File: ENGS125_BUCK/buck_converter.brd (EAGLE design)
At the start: 75.9 x 62.2 mm, 19 parts, among them M1 IPD220N06L3, M2 IPD220N06L3, U1 LTC6992, U2 LTC4449

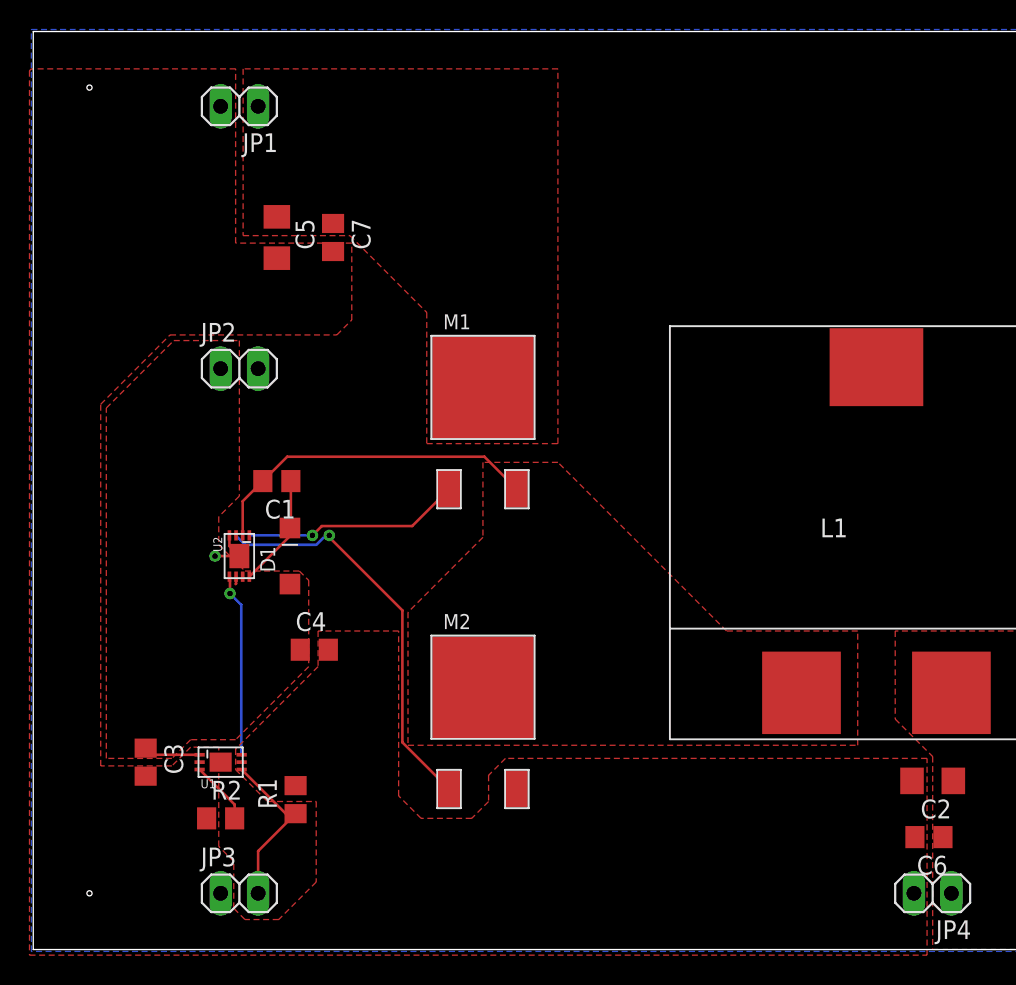
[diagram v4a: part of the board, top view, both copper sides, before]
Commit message: Cleaned up polygons and top layer routing
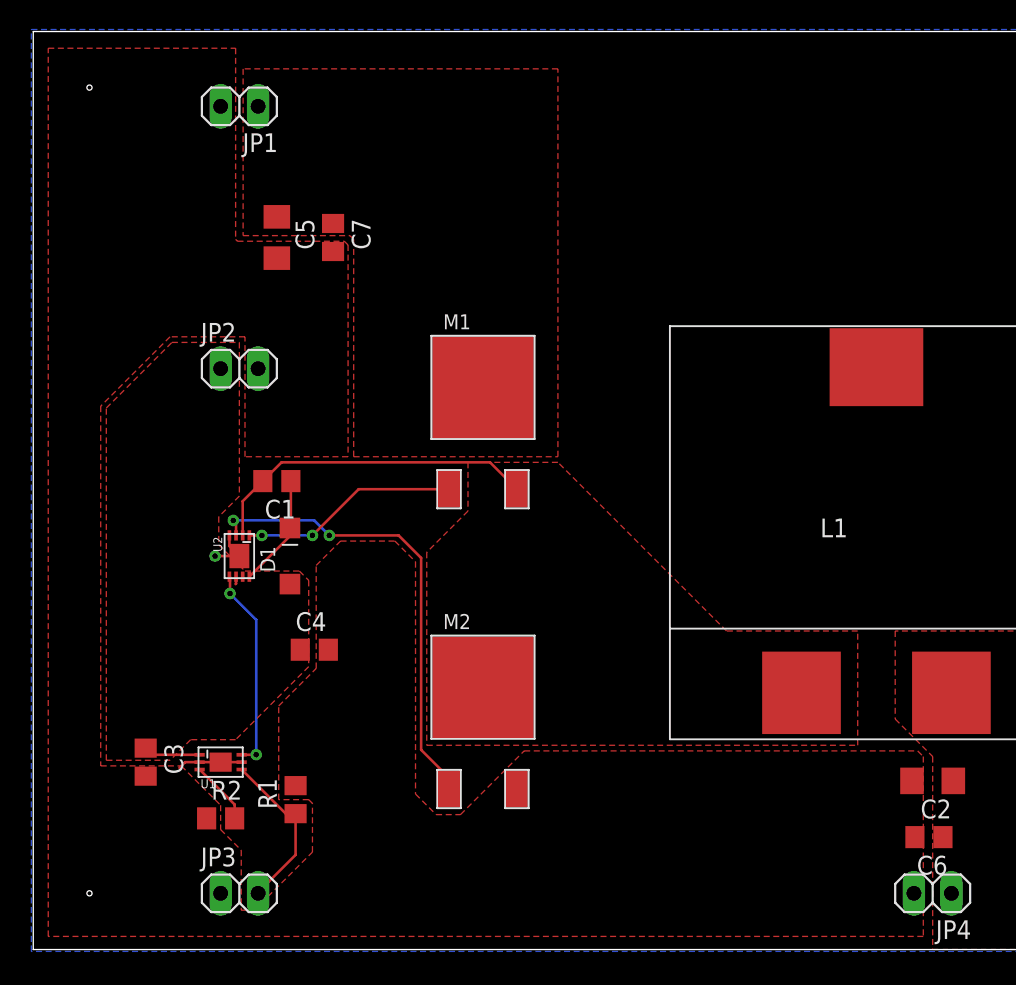
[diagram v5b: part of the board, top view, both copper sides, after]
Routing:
- net GND: track 3.33 -> 7.71 mm
- net BG: track 27.4 -> 31.3 mm, vias 1 -> 2
- net VPWM: track 12.4 -> 13.8 mm, vias 1 -> 2
- net TG: track 14.7 -> 14.8 mm, vias 1 -> 2
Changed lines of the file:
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@@
 <contactref element="U1" pad="5"/>
 <contactref element="U1" pad="7"/>
-<polygon width="0.1524" layer="1" isolate="0.00030625" thermals="no">
-<vertex x="13.716" y="47.879"/>
-<vertex x="13.716" y="59.69"/>
-<vertex x="-0.127" y="59.69"/>
-<vertex x="-0.254" y="59.563"/>
-<vertex x="-0.254" y="-0.381"/>
-<vertex x="60.579" y="-0.381"/>
-<vertex x="60.579" y="12.954"/>
-<vertex x="32.004" y="12.954"/>
-<vertex x="30.861" y="11.811"/>
-<vertex x="30.861" y="10.033"/>
-<vertex x="29.718" y="8.89"/>
-<vertex x="26.289" y="8.89"/>
-<vertex x="24.765" y="10.414"/>
-<vertex x="24.765" y="21.59"/>
-<vertex x="19.304" y="21.59"/>
-<vertex x="19.304" y="19.177"/>
-<vertex x="13.716" y="13.589"/>
-<vertex x="13.716" y="12.192"/>
-<vertex x="15.875" y="10.033"/>
-<vertex x="19.177" y="10.033"/>
-<vertex x="19.177" y="4.572"/>
-<vertex x="16.637" y="2.032"/>
-<vertex x="14.351" y="2.032"/>
-<vertex x="13.589" y="2.794"/>
-<vertex x="13.589" y="5.969"/>
-<vertex x="12.573" y="6.985"/>
-<vertex x="12.573" y="13.716"/>
-<vertex x="10.668" y="13.716"/>
-<vertex x="9.398" y="12.446"/>
-<vertex x="4.572" y="12.446"/>
-<vertex x="4.572" y="36.957"/>
-<vertex x="9.271" y="41.656"/>
-<vertex x="20.574" y="41.656"/>
-<vertex x="21.59" y="42.672"/>
-<vertex x="21.59" y="47.879"/>
-</polygon>
 <polygon width="0.1524" layer="16" isolate="0.00030625" thermals="no">
 <vertex x="-0.127" y="62.357"/>
@@
 <wire x1="13.97" y1="26.67" x2="12.319" y2="26.67" width="0.1778" layer="1"/>
 <via x="12.319" y="26.67" extent="1-16" drill="0.381"/>
+<polygon width="0.1778" layer="1" isolate="0.00030625" thermals="no">
+<vertex x="60.325" y="13.081"/>
+<vertex x="60.325" y="0.889"/>
+<vertex x="1.016" y="0.889"/>
+<vertex x="1.016" y="61.087"/>
+<vertex x="13.716" y="61.087"/>
+<vertex x="13.716" y="48.133"/>
+<vertex x="13.843" y="48.006"/>
+<vertex x="21.082" y="48.006"/>
+<vertex x="21.336" y="47.752"/>
+<vertex x="21.336" y="33.401"/>
+<vertex x="14.351" y="33.401"/>
+<vertex x="14.351" y="41.529"/>
+<vertex x="9.271" y="41.529"/>
+<vertex x="4.572" y="36.83"/>
+<vertex x="4.572" y="12.446"/>
+<vertex x="10.033" y="12.446"/>
+<vertex x="12.7" y="9.779"/>
+<vertex x="12.7" y="8.128"/>
+<vertex x="14.097" y="6.731"/>
+<vertex x="14.097" y="2.667"/>
+<vertex x="14.986" y="2.667"/>
+<vertex x="18.923" y="6.604"/>
+<vertex x="18.923" y="9.906"/>
+<vertex x="18.669" y="10.16"/>
+<vertex x="16.637" y="10.16"/>
+<vertex x="16.637" y="16.51"/>
+<vertex x="19.177" y="19.05"/>
+<vertex x="19.177" y="26.035"/>
+<vertex x="20.828" y="27.686"/>
+<vertex x="24.511" y="27.686"/>
+<vertex x="25.908" y="26.289"/>
+<vertex x="25.908" y="10.541"/>
+<vertex x="27.305" y="9.144"/>
+<vertex x="28.956" y="9.144"/>
+<vertex x="33.274" y="13.462"/>
+<vertex x="59.944" y="13.462"/>
+</polygon>
+<wire x1="11.275" y1="12.7" x2="10.287" y2="12.7" width="0.1778" layer="1"/>
+<wire x1="10.287" y1="12.7" x2="9.906" y2="12.319" width="0.1778" layer="1"/>
+<wire x1="14.125" y1="12.7" x2="12.7" y2="12.7" width="0.1778" layer="1"/>
+<wire x1="12.7" y1="12.7" x2="11.275" y2="12.7" width="0.1778" layer="1"/>
 </signal>
 <signal name="VGG">
@@
 <contactref element="U2" pad="6"/>
 <polygon width="0.1778" layer="1" isolate="0.00030625" thermals="no">
-<vertex x="13.97" y="41.275"/>
+<vertex x="13.97" y="41.148"/>
 <vertex x="13.97" y="30.734"/>
 <vertex x="12.573" y="29.337"/>
@@
 <vertex x="13.716" y="14.224"/>
 <vertex x="10.668" y="14.224"/>
-<vertex x="9.398" y="12.954"/>
-<vertex x="4.953" y="12.954"/>
+<vertex x="9.271" y="12.827"/>
+<vertex x="4.953" y="12.827"/>
 <vertex x="4.953" y="36.703"/>
-<vertex x="9.525" y="41.275"/>
+<vertex x="9.398" y="41.148"/>
 </polygon>
 <wire x1="13.745" y1="25.27" x2="13.745" y2="24.794" width="0.1778" layer="1"/>
@@
 <wire x1="13.295" y1="25.27" x2="13.335" y2="25.23" width="0.1778" layer="1"/>
 <via x="13.335" y="24.13" extent="1-16" drill="0.381"/>
-<wire x1="13.335" y1="24.13" x2="14.097" y2="23.368" width="0.1778" layer="16"/>
-<wire x1="14.097" y1="23.368" x2="14.097" y2="13.208" width="0.1778" layer="16"/>
+<wire x1="13.335" y1="24.13" x2="15.113" y2="22.352" width="0.1778" layer="16"/>
+<wire x1="15.113" y1="22.352" x2="15.113" y2="13.208" width="0.1778" layer="16"/>
 <wire x1="13.335" y1="25.23" x2="13.335" y2="24.13" width="0.1778" layer="1"/>
-<wire x1="14.097" y1="13.208" x2="14.125" y2="13.2" width="0" layer="19" extent="1-16"/>
+<via x="15.113" y="13.208" extent="1-16" drill="0.381"/>
+<wire x1="15.113" y1="13.208" x2="15.105" y2="13.2" width="0.1778" layer="1"/>
+<wire x1="15.105" y1="13.2" x2="14.125" y2="13.2" width="0.1778" layer="1"/>
 </signal>
 <signal name="VMOD">
@@
 <contactref element="R1" pad="1"/>
 <contactref element="JP3" pad="2"/>
-<wire x1="15.24" y1="3.81" x2="15.24" y2="6.67" width="0.1778" layer="1"/>
-<wire x1="15.24" y1="6.67" x2="17.78" y2="9.21" width="0.1778" layer="1"/>
+<wire x1="15.24" y1="3.81" x2="15.24" y2="3.876" width="0.1778" layer="1"/>
+<wire x1="17.78" y1="6.416" x2="15.24" y2="3.876" width="0.1778" layer="1"/>
+<wire x1="17.78" y1="6.416" x2="17.78" y2="9.21" width="0.1778" layer="1"/>
 <wire x1="14.125" y1="12.2" x2="17.115" y2="9.21" width="0.1778" layer="1"/>
 <wire x1="17.115" y1="9.21" x2="17.78" y2="9.21" width="0.1778" layer="1"/>
@@
 <contactref element="U2" pad="2"/>
 <polygon width="0.1524" layer="1" isolate="0.00030625" thermals="no">
-<vertex x="25.4" y="22.86"/>
-<vertex x="25.4" y="13.843"/>
+<vertex x="26.67" y="26.924"/>
+<vertex x="26.67" y="13.843"/>
 <vertex x="55.88" y="13.843"/>
 <vertex x="55.88" y="21.59"/>
 <vertex x="46.99" y="21.59"/>
 <vertex x="35.56" y="33.02"/>
-<vertex x="30.48" y="33.02"/>
-<vertex x="30.48" y="27.94"/>
+<vertex x="29.464" y="33.02"/>
+<vertex x="29.464" y="29.718"/>
 </polygon>
-<wire x1="32.78" y1="31.2" x2="30.579" y2="33.401" width="0.1778" layer="1"/>
-<wire x1="30.579" y1="33.401" x2="17.211" y2="33.401" width="0.1778" layer="1"/>
-<wire x1="17.211" y1="33.401" x2="15.56" y2="31.75" width="0.1778" layer="1"/>
+<wire x1="32.78" y1="31.2" x2="30.96" y2="33.02" width="0.1778" layer="1"/>
+<wire x1="30.96" y1="33.02" x2="16.83" y2="33.02" width="0.1778" layer="1"/>
+<wire x1="16.83" y1="33.02" x2="15.56" y2="31.75" width="0.1778" layer="1"/>
 <wire x1="15.56" y1="31.75" x2="14.195" y2="30.385" width="0.1778" layer="1"/>
 <wire x1="14.195" y1="30.385" x2="14.195" y2="28.07" width="0.1778" layer="1"/>
@@
 <vertex x="14.224" y="48.387"/>
 <vertex x="21.463" y="48.387"/>
-<vertex x="26.67" y="43.18"/>
-<vertex x="26.67" y="34.29"/>
-<vertex x="35.56" y="34.29"/>
+<vertex x="21.717" y="48.133"/>
+<vertex x="21.717" y="33.401"/>
+<vertex x="35.56" y="33.401"/>
 <vertex x="35.56" y="59.69"/>
 </polygon>
@@
 <contactref element="U2" pad="3"/>
 <contactref element="M2" pad="G"/>
-<wire x1="28.18" y1="10.88" x2="25.019" y2="14.041" width="0.1778" layer="1"/>
-<wire x1="25.019" y1="14.041" x2="25.019" y2="22.987" width="0.1778" layer="1"/>
-<wire x1="25.019" y1="22.987" x2="20.066" y2="27.94" width="0.1778" layer="1"/>
-<wire x1="20.066" y1="27.94" x2="20.066" y2="28.067" width="0.1778" layer="1"/>
+<wire x1="28.18" y1="10.88" x2="28.18" y2="11.642" width="0.1778" layer="1"/>
+<wire x1="28.18" y1="11.642" x2="26.289" y2="13.533" width="0.1778" layer="1"/>
+<wire x1="26.289" y1="13.533" x2="26.289" y2="26.543" width="0.1778" layer="1"/>
+<wire x1="20.066" y1="28.067" x2="24.765" y2="28.067" width="0.1778" layer="1"/>
+<wire x1="26.289" y1="26.543" x2="24.765" y2="28.067" width="0.1778" layer="1"/>
 <via x="20.066" y="28.067" extent="1-16" drill="0.381"/>
-<wire x1="20.066" y1="28.067" x2="19.82103125" y2="28.067" width="0.1778" layer="16"/>
-<wire x1="19.82103125" y1="28.067" x2="19.18603125" y2="27.432" width="0.1778" layer="16"/>
-<wire x1="19.18603125" y1="27.432" x2="14.351" y2="27.432" width="0.1778" layer="16"/>
-<wire x1="14.351" y1="27.432" x2="13.716" y2="28.067" width="0.1778" layer="16"/>
-<wire x1="13.716" y1="28.067" x2="13.745" y2="28.07" width="0" layer="19" extent="1-16"/>
+<wire x1="20.066" y1="28.067" x2="19.05" y2="29.083" width="0.1778" layer="16"/>
+<via x="13.56" y="29.083" extent="1-16" drill="0.381"/>
+<wire x1="13.56" y1="29.083" x2="13.745" y2="28.898" width="0.1778" layer="1"/>
+<wire x1="13.745" y1="28.898" x2="13.745" y2="28.07" width="0.1778" layer="1"/>
+<wire x1="19.05" y1="29.083" x2="13.56" y2="29.083" width="0.1778" layer="16"/>
 </signal>
 <signal name="TG">
 <contactref element="U2" pad="1"/>
 <contactref element="M1" pad="G"/>
-<wire x1="28.18" y1="31.2" x2="25.682" y2="28.702" width="0.1778" layer="1"/>
-<wire x1="18.923" y1="28.067" x2="19.558" y2="28.702" width="0.1778" layer="1"/>
-<wire x1="25.682" y1="28.702" x2="19.558" y2="28.702" width="0.1778" layer="1"/>
+<wire x1="28.18" y1="31.2" x2="22.056" y2="31.2" width="0.1778" layer="1"/>
+<wire x1="22.056" y1="31.2" x2="18.923" y2="28.067" width="0.1778" layer="1"/>
 <via x="18.923" y="28.067" extent="1-16" drill="0.381"/>
-<wire x1="18.923" y1="28.067" x2="14.732" y2="28.067" width="0.1778" layer="16"/>
-<wire x1="14.732" y1="28.067" x2="14.645" y2="28.07" width="0" layer="19" extent="1-16"/>
+<wire x1="18.923" y1="28.067" x2="15.494" y2="28.067" width="0.1778" layer="16"/>
+<via x="15.494" y="28.067" extent="1-16" drill="0.381"/>
+<wire x1="15.494" y1="28.067" x2="14.648" y2="28.067" width="0.1778" layer="1"/>
+<wire x1="14.648" y1="28.067" x2="14.645" y2="28.07" width="0.1778" layer="1"/>
 </signal>
 </signals>
